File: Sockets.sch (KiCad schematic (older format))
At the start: 44 parts, among them J10 CA58SUB-B, J11 PC6 EPSON MAINBOARD, J12 WASTE INK, J13 LED 1, J14 LED 2, J15 Y AXIS, J16 Z AXIS, J6 LIMIT Z UP, J7 LIMIT Z DOWN, J8 LIMIT Y BACK, J9 LIMIT Y FRONT, Q2 BC817, Q3 BC817, U5 74HC245

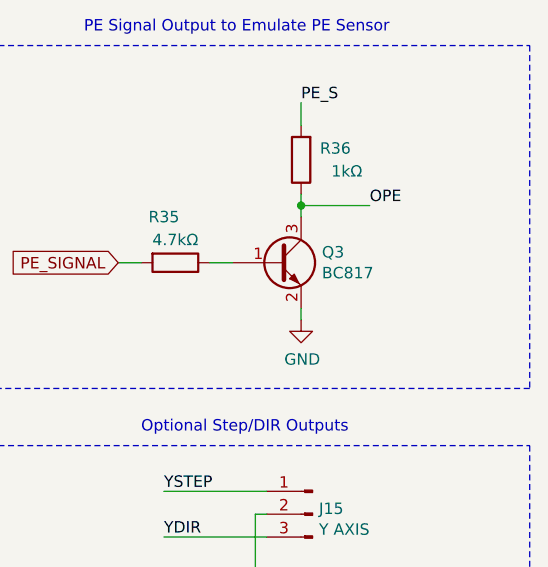
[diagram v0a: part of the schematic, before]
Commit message: Improve Emergency, Added TVS diodes
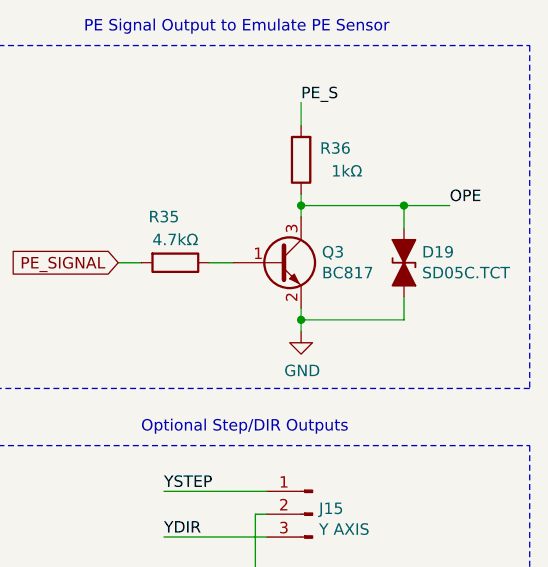
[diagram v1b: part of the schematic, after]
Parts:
- added D19: SD05C.TCT, Diode_SMD:D_SOD-323, symbol Device:D_TVS_ALT
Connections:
- net GND: now also D19.2 (A2)
- net OPE: now also D19.1 (A1)

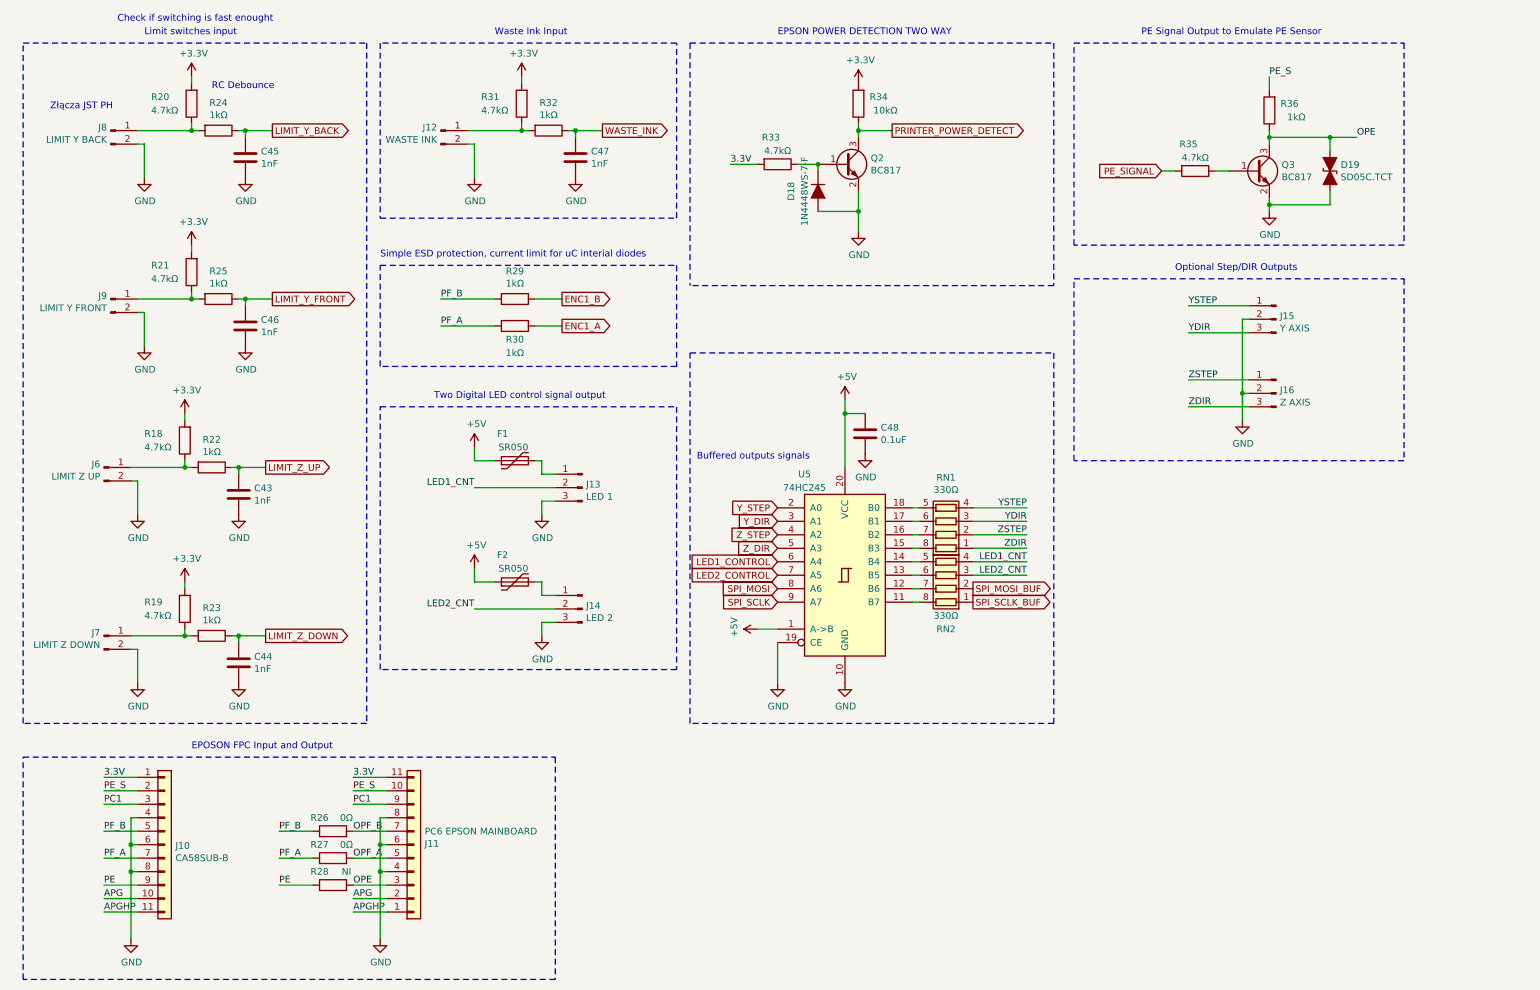
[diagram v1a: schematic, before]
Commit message: Added 12V regulator, aditional input, outputs, improved inputs ESD
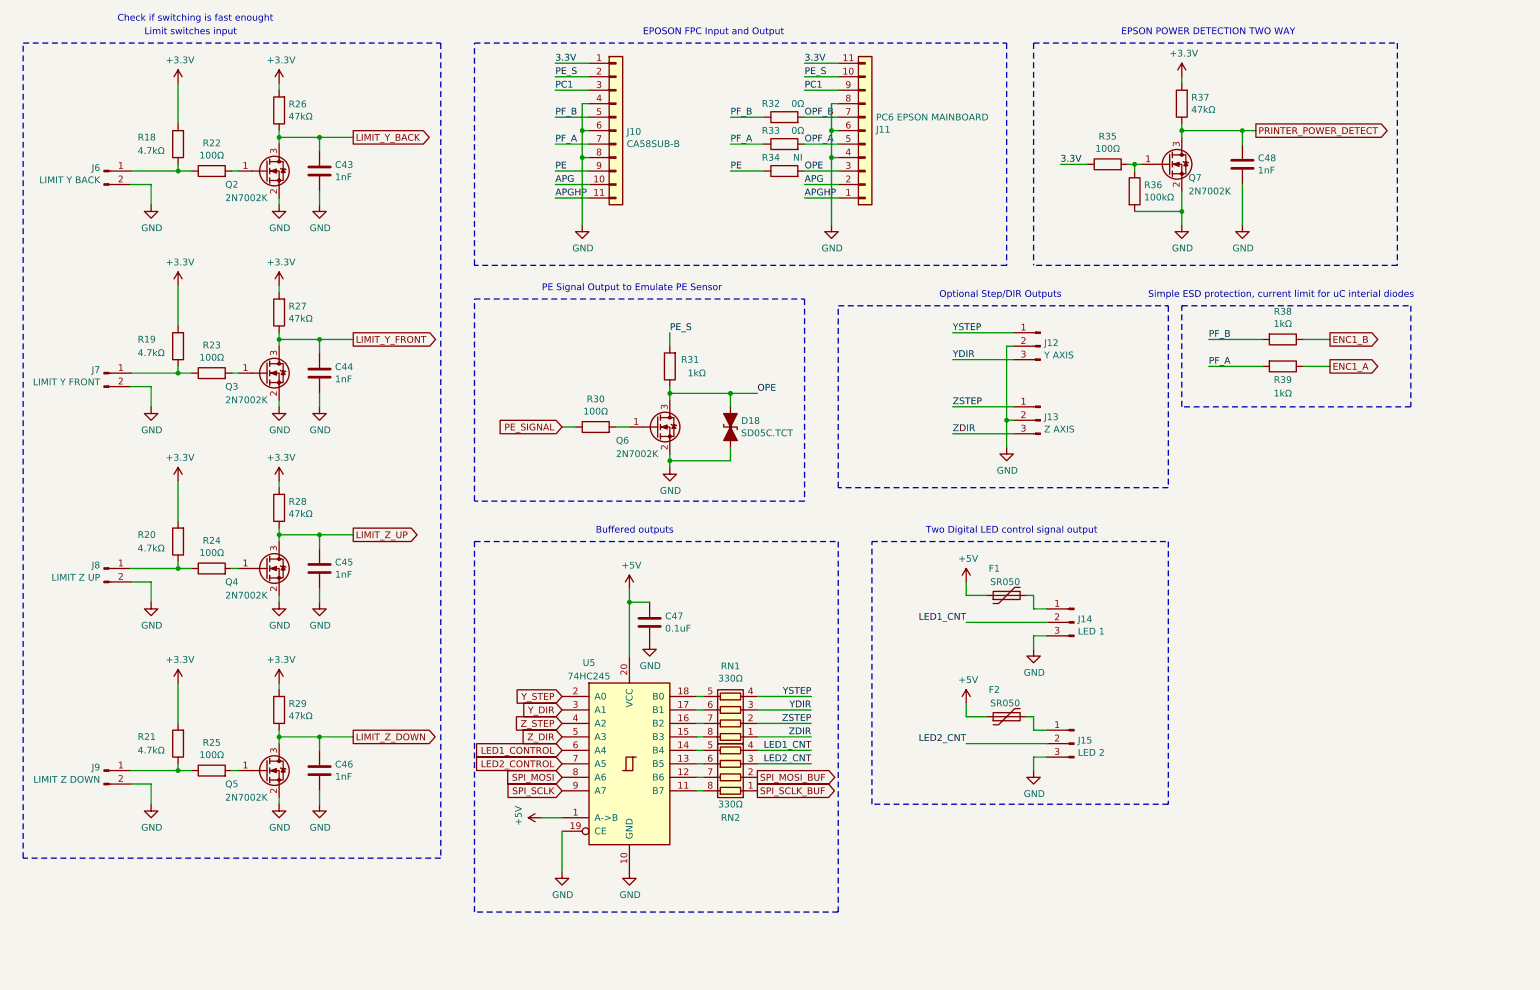
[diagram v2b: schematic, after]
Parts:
- removed C47: 1nF, Capacitor_SMD:C_0603_1608Metric, symbol Device:C
- removed D18: 1N4448WS-7-F, Diode_SMD:D_SOD-323, symbol Device:D_ALT
- removed J12: WASTE INK, Connector_JST:JST_PH_B2B-PH-K_1x02_P2.00mm_Vertical, symbol Connector:Conn_01x02_Male
- removed Q2, Q3: BC817, Package_TO_SOT_SMD:SOT-23, symbol Transistor_BJT:BC817
- removed R31, R33: 4.7kΩ, Resistor_SMD:R_0603_1608Metric, symbol Device:R
- removed R32: 1kΩ, Resistor_SMD:R_0603_1608Metric, symbol Device:R
- removed R34: 10kΩ, Resistor_SMD:R_0603_1608Metric, symbol Device:R
- added C48: 1nF, Capacitor_SMD:C_0603_1608Metric, symbol Device:C
- added Q2, Q3, Q4, Q5, Q6, Q7: 2N7002K, Package_TO_SOT_SMD:SOT-23, symbol Transistor_FET:2N7002K
- added R26, R27, R28, R29, R37: 47kΩ, Resistor_SMD:R_0603_1608Metric, symbol Device:R
- added R30: 100Ω, Resistor_SMD:R_0603_1608Metric, symbol Device:R
- added R36: 100kΩ, Resistor_SMD:R_0603_1608Metric, symbol Device:R
- J6: value LIMIT Z UP -> LIMIT Y BACK
- J7: value LIMIT Z DOWN -> LIMIT Y FRONT
- J8: value LIMIT Y BACK -> LIMIT Z UP
- J9: value LIMIT Y FRONT -> LIMIT Z DOWN
- R22, R23, R24, R25: value 1kΩ -> 100Ω; Cena 0.04651 -> (none); Link https://www.tme.eu/pl/details/smd0603-1k-1%25/rezystory-smd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 -> (none); Model 0603SAF1001T5E -> (none); Opis Rezystor: thick film; SMD; 0603; 1kΩ; 0,1W; ±1%; -55÷155°C -> (none); Producent ROYAL OHM -> (none); Typ SMD -> (none)
- R35: value 4.7kΩ -> 100Ω; Cena 0.04651 -> (none); Link https://www.tme.eu/pl/details/smd0603-4k7-1%25/rezystory-sm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 -> (none); Model SMD0603-4K7-1% -> (none); Opis Rezystor: thick film; SMD; 0603; 4,7kΩ; 0,1W; ±1%; -55÷155°C -> (none); Producent ROYAL OHM -> (none); Typ SMD -> (none)
- renumbered C48 to C47, D19 to D18, J15 to J12, J16 to J13, J13 to J14, J14 to J15, R36 to R31, R26 to R32, R27 to R33, R28 to R34, R29 to R38, R30 to R39
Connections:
- net +3V3: now also R26.2, R27.2, R28.2, R29.2, R37.2
- net 3.3V: now also R35.1
- net GND: now also C48.2, Q2.2 (S), Q3.2 (S), Q4.2 (S), Q5.2 (S), Q6.2 (S), Q7.2 (S), R36.2
- net LIMIT_Y_BACK: now also C43.1, Q2.3 (D), R26.1; no longer C45.1, R24.1
- net LIMIT_Y_FRONT: now also C44.1, Q3.3 (D), R27.1; no longer C46.1, R25.1
- net LIMIT_Z_DOWN: now also C46.1, Q5.3 (D), R29.1; no longer C44.1, R23.1
- net LIMIT_Z_UP: now also C45.1, Q4.3 (D), R28.1; no longer C43.1, R22.1
- net OPE: now also Q6.3 (D)
- net PE_SIGNAL: now also R30.1; no longer R35.2
- net PRINTER_POWER_DETECT: now also C48.1, Q7.3 (D), R37.1
- net at J8.1 (Pin_1), R20.1: now also R24.1; no longer R24.2
- net at J9.1 (Pin_1), R21.1: now also R25.1; no longer R25.2
- net at J6.1 (Pin_1), R18.1: now also R22.1; no longer R22.2
- net at J7.1 (Pin_1), R19.1: now also R23.1; no longer R23.2
- new net: Q2.1 (G), R22.2
- new net: Q3.1 (G), R23.2
- new net: Q4.1 (G), R24.2
- new net: Q5.1 (G), R25.2
- new net: Q7.1 (G), R35.2, R36.1
- new net: Q6.1 (G), R30.2
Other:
- note added: "Buffered outputs"
- note removed: "Buffered outputs signals"
- note removed: "RC Debounce"
- note removed: "Waste Ink Input"
- note removed: "Złącza JST PH"
- moved on the sheet: C47, D18, F1, F2, J10, J11, J12, J13, J14, J15, R31, R32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

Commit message: Added analog input
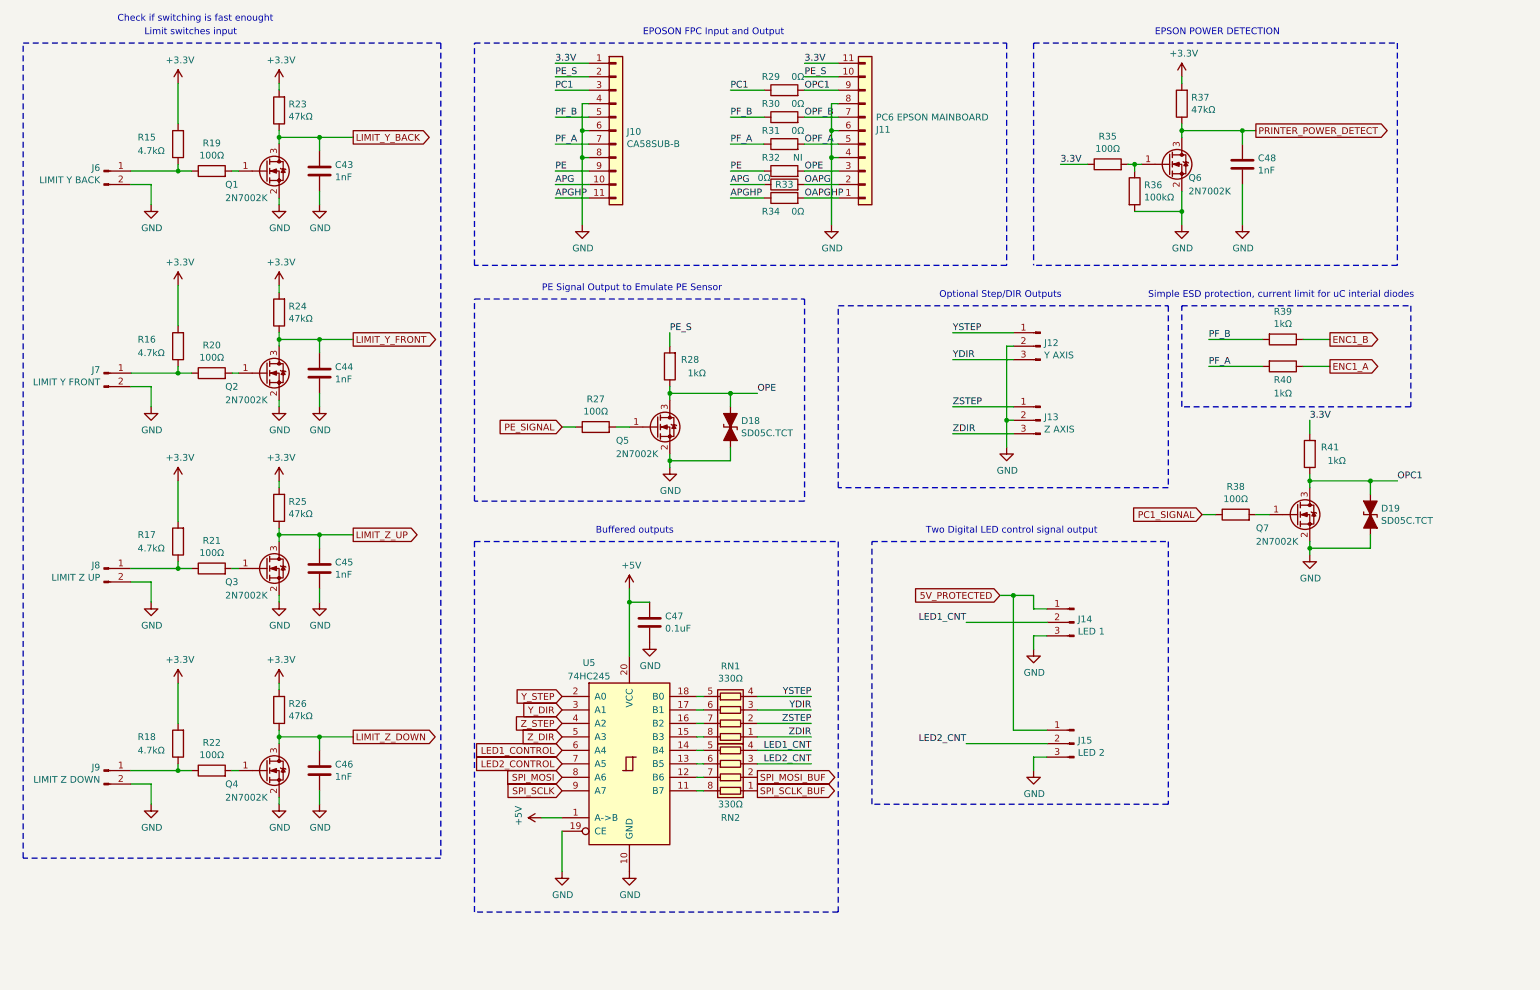
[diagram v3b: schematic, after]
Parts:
- removed F1, F2: SR050, Fuse:Fuse_0805_2012Metric, symbol Device:Polyfuse
- added D19: SD05C.TCT, Diode_SMD:D_SOD-323, symbol Device:D_TVS_ALT
- added Q7: 2N7002K, Package_TO_SOT_SMD:SOT-23, symbol Transistor_FET:2N7002K
- added R29, R33, R34: 0Ω, Resistor_SMD:R_0603_1608Metric, symbol Device:R
- added R38: 100Ω, Resistor_SMD:R_0603_1608Metric, symbol Device:R
- added R41: 1kΩ, Resistor_SMD:R_0603_1608Metric, symbol Device:R
- renumbered Q2 to Q1, Q3 to Q2, Q4 to Q3, Q5 to Q4, Q6 to Q5, Q7 to Q6, R18 to R15, R19 to R16, R20 to R17, R21 to R18, R22 to R19, R23 to R20, R24 to R21, R25 to R22, R26 to R23, R27 to R24, R28 to R25, R29 to R26, R30 to R27, R31 to R28, R32 to R30, R33 to R31, R34 to R32, R38 to R39, R39 to R40
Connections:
- net 3.3V: now also R41.2
- net APG: now also R33.1; no longer J11.2 (Pin_2)
- net APGHP: now also R34.1; no longer J11.1 (Pin_1)
- net GND: now also D19.2 (A2), Q7.2 (S)
- net PC1: now also R29.1; no longer J11.9 (Pin_9)
- net 5V_PROTECTED: now reaches J14.1 (Pin_1)
- net 5V_PROTECTED: now also J15.1 (Pin_1)
- new net: Q7.1 (G), R38.2
- new net OAPG: J11.2 (Pin_2), R33.2
- new net OAPGHP: J11.1 (Pin_1), R34.2
- new net OPC1: D19.1 (A1), J11.9 (Pin_9), Q7.3 (D), R29.2, R41.1
- new net PC1_SIGNAL: R38.1
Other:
- note added: "EPSON POWER DETECTION"
- note removed: "EPSON POWER DETECTION TWO WAY"

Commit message: Improve ESD Protection for TMC2209, Fuses. Schematic ready v1
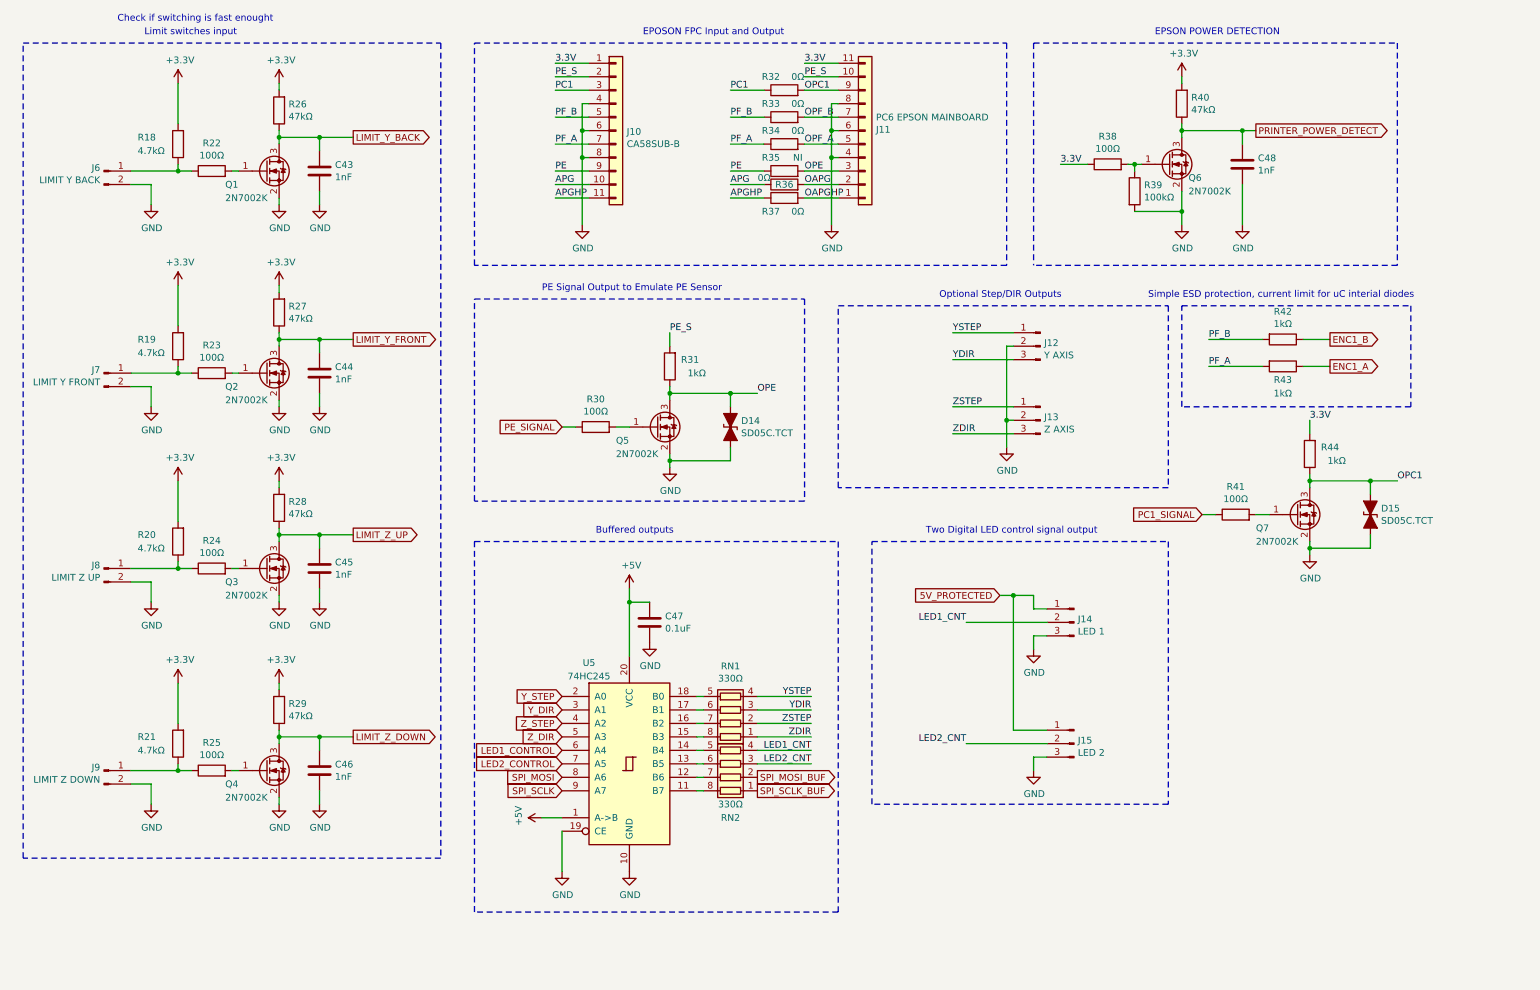
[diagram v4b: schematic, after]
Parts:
- renumbered D18 to D14, D19 to D15, R15 to R18, R16 to R19, R17 to R20, R18 to R21, R19 to R22, R20 to R23, R21 to R24, R22 to R25, R23 to R26, R24 to R27, R25 to R28, R26 to R29, R27 to R30, R28 to R31, R29 to R32, R30 to R33, R31 to R34, R32 to R35, R33 to R36, R34 to R37, R35 to R38, R36 to R39, R37 to R40, R38 to R41, R39 to R42, R40 to R43, R41 to R44

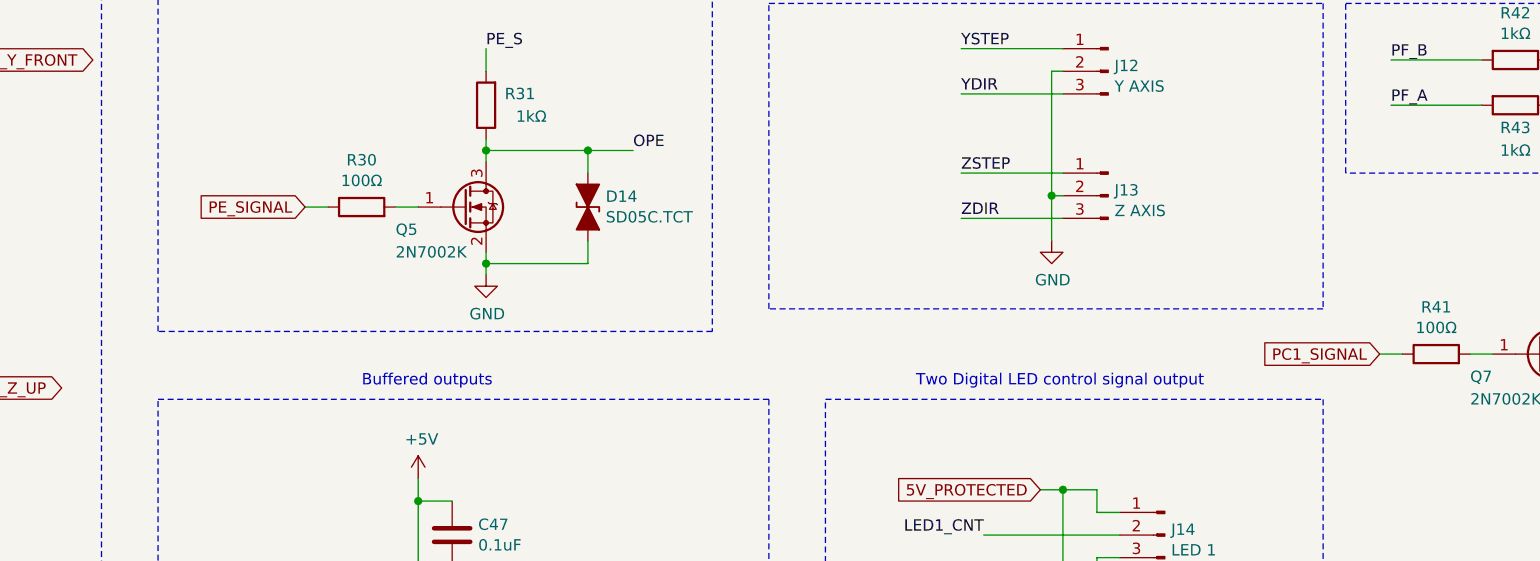
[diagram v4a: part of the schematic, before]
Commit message: Modify pin attribute, routing keys input
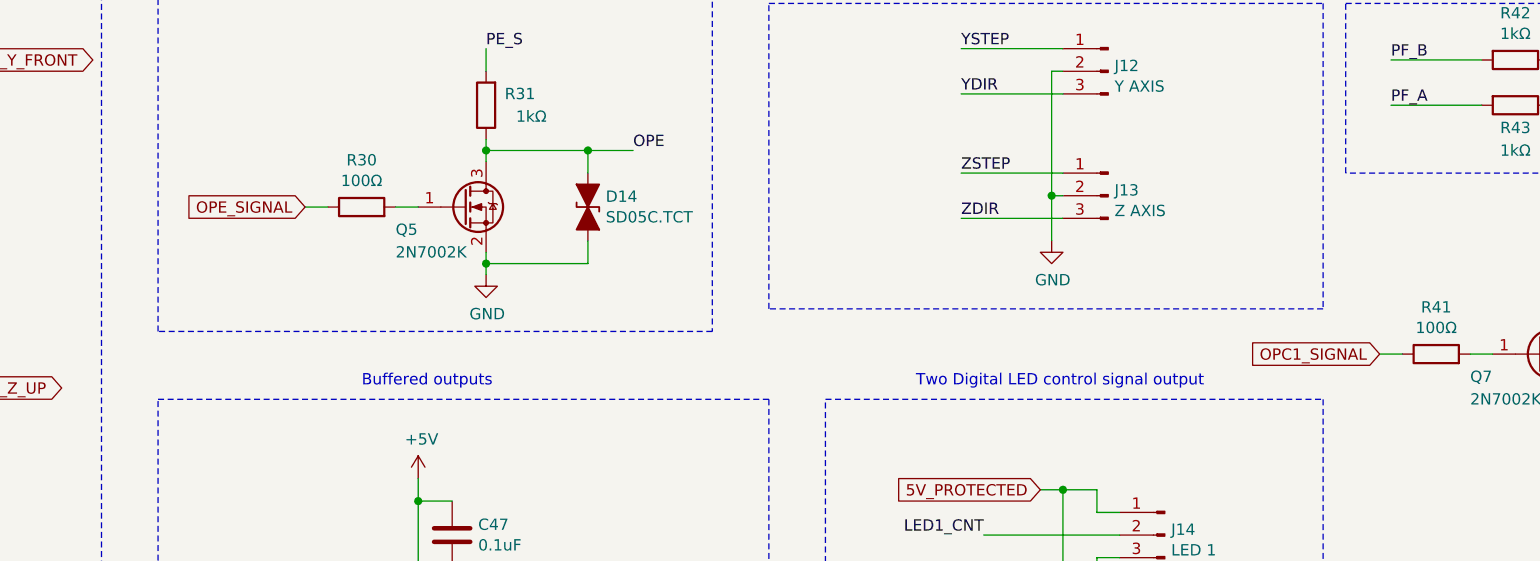
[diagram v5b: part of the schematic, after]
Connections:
- net PC1_SIGNAL renamed OPC1_SIGNAL
- net PE_SIGNAL renamed OPE_SIGNAL
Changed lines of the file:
@@
 OPE
 Text GLabel 4700 3600 0    50   Input ~ 0
-PE_SIGNAL
+OPE_SIGNAL
 Text Label 9500 2950 0    50   ~ 0
 PF_B
@@
 OPC1
 Text GLabel 9450 4250 0    50   Input ~ 0
-PC1_SIGNAL
+OPC1_SIGNAL
 Wire Wire Line
 	10700 4100 10700 4000
